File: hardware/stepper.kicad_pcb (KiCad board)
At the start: 4 copper layers, 40 x 40 mm, 125 parts, among them J101 USB-MINI-B-SMD, J102 DRILL, J103 DRILL, J104 DRILL, J105 DRILL, J401 STACK-UP-HIGH, J402 STACK-DOWN, J403 STACK-UP-HIGH, J404 STACK-DOWN, P201 black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

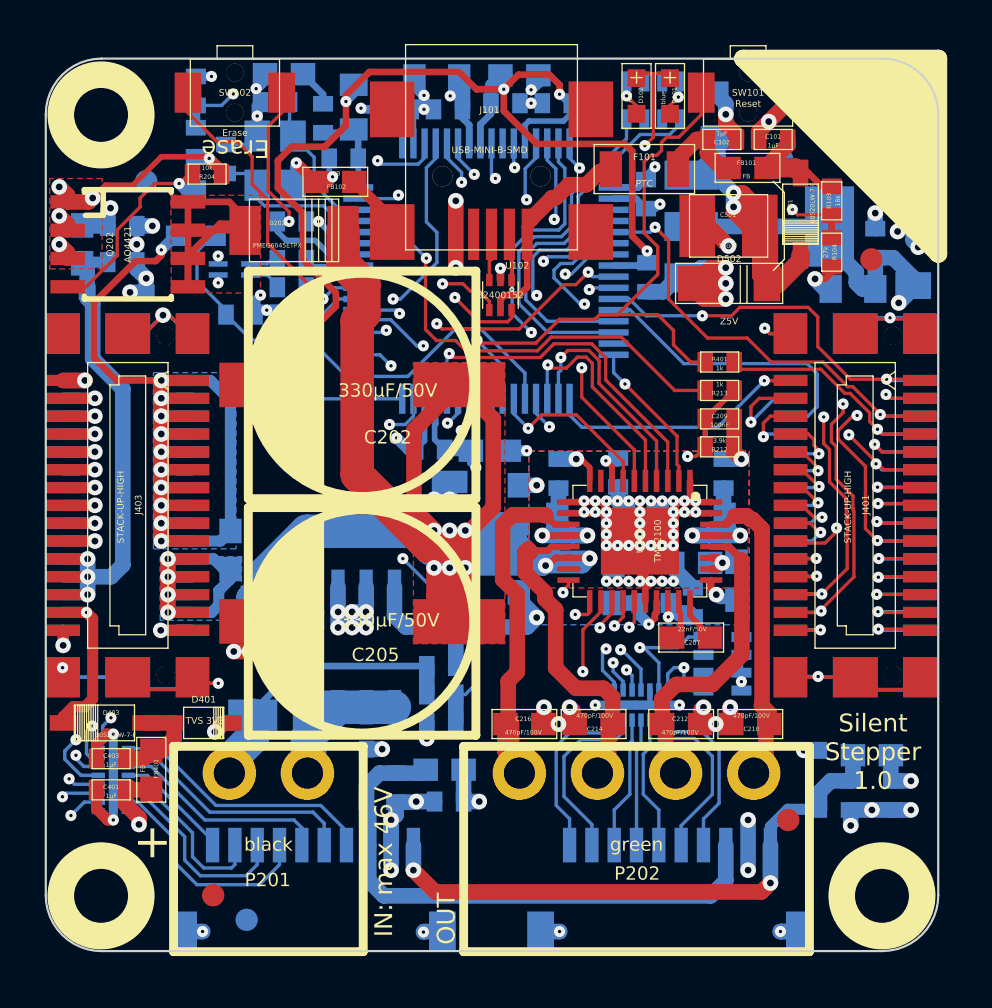
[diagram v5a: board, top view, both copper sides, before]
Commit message: remove motor capacitors
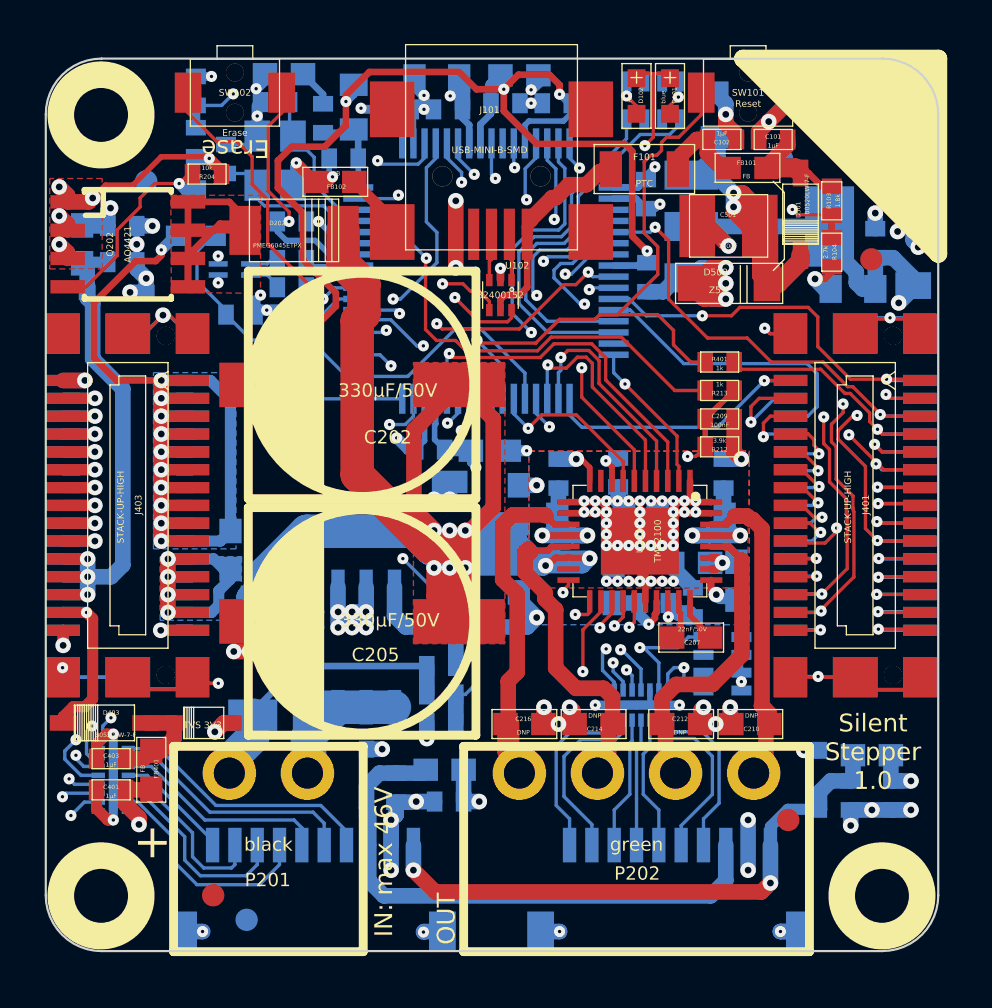
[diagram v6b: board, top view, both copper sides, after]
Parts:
- C210, C212, C214, C216: value 470pF/100V -> DNP
- R103: value 18k -> 1.8k
- R104: value 27k -> 2.7k
- turned D301 to 270 degrees
- turned D302 to 270 degrees
- turned D401 to 180 degrees
- turned D402 to 180 degrees
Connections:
- D301 pad 1: Net-(C303-Pad1) -> GND
- D301 pad 2: GND -> Net-(C303-Pad1)
- D302 pad 1: Net-(C304-Pad1) -> GND
- D302 pad 2: GND -> Net-(C304-Pad1)
- D401 pad 1: Net-(C403-Pad1) -> GND
- D401 pad 2: GND -> Net-(C403-Pad1)
- D402 pad 1: Net-(C404-Pad1) -> GND
- D402 pad 2: GND -> Net-(C404-Pad1)
- FILTER301 pad 8: Net-(FILTER301-Pad8) -> (no net)
- FILTER301 pad 9: Net-(FILTER301-Pad9) -> (no net)
- FILTER302 pad 8: Net-(FILTER302-Pad8) -> (no net)
- FILTER302 pad 9: Net-(FILTER302-Pad9) -> (no net)
- J101 pad 4: Net-(J101-Pad4) -> (no net)
- RP101 pad 2: Net-(RP101-Pad2) -> (no net)
- RP101 pad 3: Net-(RP101-Pad3) -> (no net)
- RP101 pad 6: Net-(RP101-Pad6) -> (no net)
- RP101 pad 7: Net-(RP101-Pad7) -> (no net)
- RP301 pad 6: Net-(RP301-Pad6) -> (no net)
- RP301 pad 7: Net-(RP301-Pad7) -> (no net)
- U101 pad 10: Net-(U101-Pad10) -> (no net)
- U101 pad 31: Net-(U101-Pad31) -> (no net)
- U101 pad 40: Net-(U101-Pad40) -> (no net)
- U101 pad 41: Net-(U101-Pad41) -> (no net)
- U101 pad 50: Net-(U101-Pad50) -> (no net)
- U202 pad 17: Net-(U202-Pad17) -> (no net)
- U202 pad 9: Net-(U202-Pad9) -> (no net)

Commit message: uncomitted hardware changes
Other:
- board text added: "check height"
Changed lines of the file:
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@@
     (area 125.845139 71.945139 283.420502 165.440043)
     (thickness 1.6002)
-    (drawings 63)
+    (drawings 64)
     (tracks 2561)
     (zones 0)
@@
   )
   (layers
-    (0 Vorderseite signal)
+    (0 Vorderseite signal hide)
     (1 GND signal hide)
     (2 VCC signal hide)
@@
     )
   )
+  (gr_text "check height" (at 155.75 99.75) (layer F.SilkS)
+    (effects (font (size 0.29972 0.29972) (thickness 0.07493)))
+  )
   (gr_text "Silent\nStepper\n1.0" (at 163.8 103.85) (layer F.SilkS)

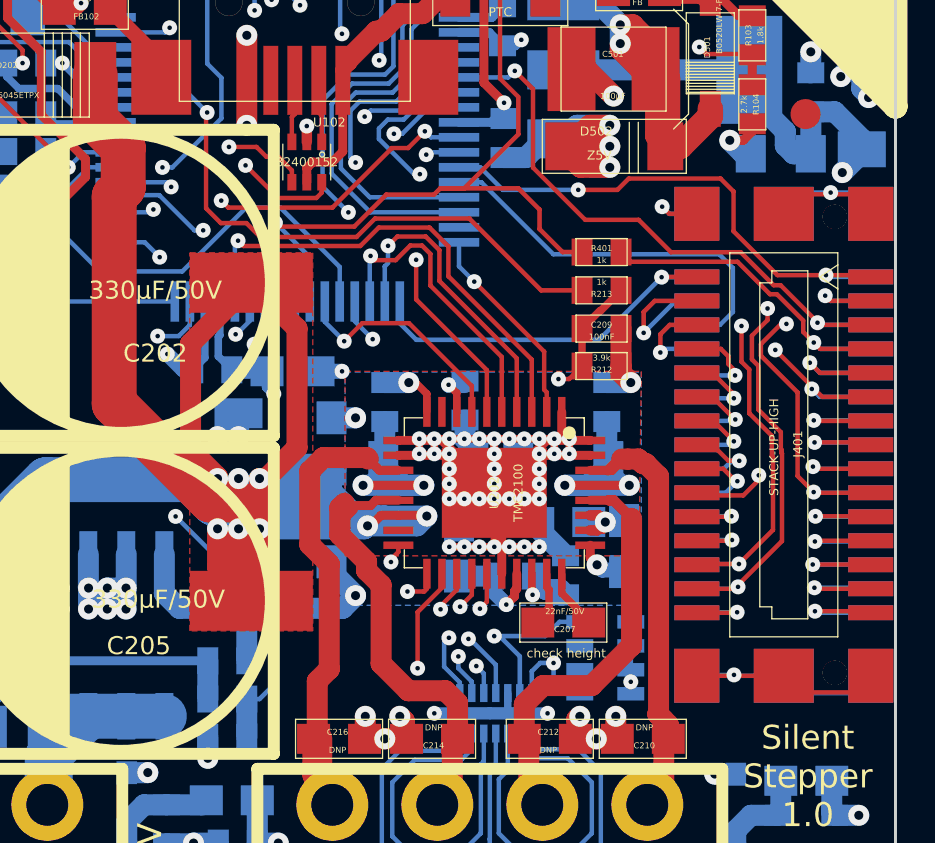
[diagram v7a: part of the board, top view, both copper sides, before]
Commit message: remove cfg3, add clk connection, imprv gnd routing, 3v3 switchable
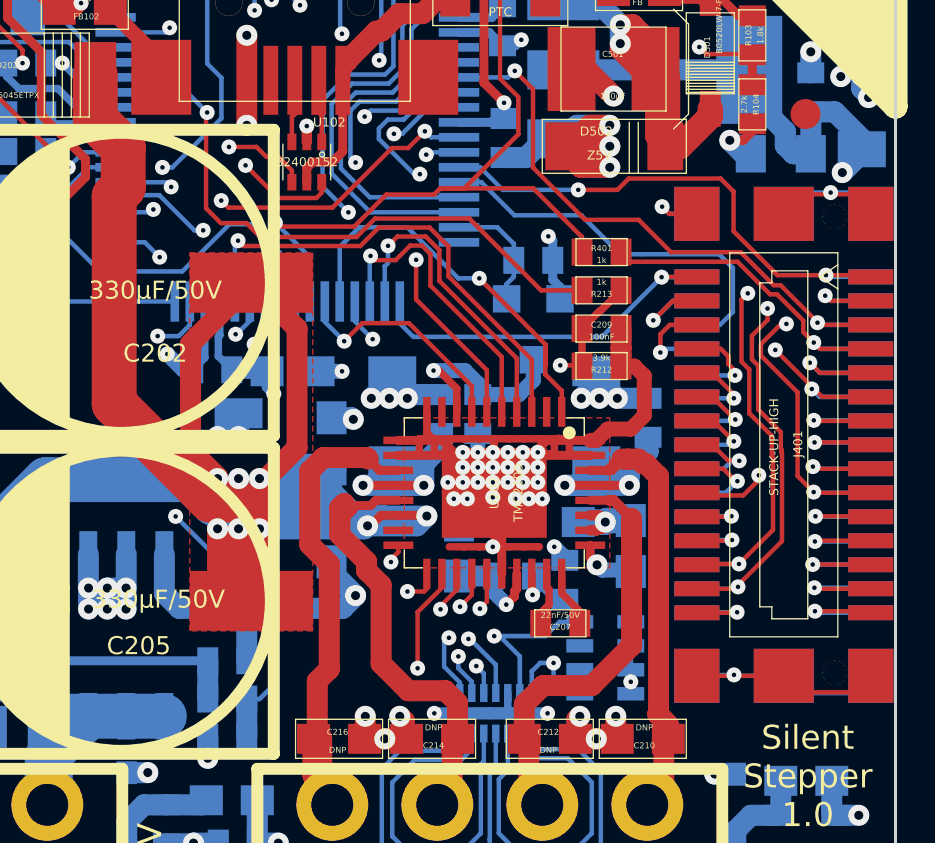
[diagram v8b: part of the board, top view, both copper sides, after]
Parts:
- added Q1: MOSFET_P, SOT23GDS, B.Cu at (154.7, 89.0)
- added R1: 10k, kicad-libraries:0402E, B.Cu at (154.7, 86.7)
- C207: footprint kicad-libraries:0603E -> kicad-libraries:0402E
- moved G*** 16.3 mm to (173.6, 82.8)
- moved R214 2.02 mm to (149.9, 91.8), turned to 270 degrees
- moved R215 1.96 mm to (156.8, 91.8), turned to 270 degrees
- moved C217 1.87 mm to (151.5, 91.8)
- moved C218 1.47 mm to (158.5, 91.9)
- moved C201 0.62 mm to (152.8, 91.8)
- moved C211 0.35 mm to (155.3, 95.4)
- moved C208 0.22 mm to (157.9, 96.2)
- moved C203 0.15 mm to (155.7, 97.3)
- moved C207 0.10 mm to (155.6, 98.8)
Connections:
- C201 pad 2: 3V3 -> Net-(C201-Pad2)
- U101 pad 31: (no net) -> PWR-SW-3V3
- U101 pad 32: PWR-CFG3 -> (no net)
- U101 pad 37: PWR-VSTACK-SW -> PWR-CLK
- U101 pad 41: (no net) -> PWR-VSTACK-SW
- U202 pad 1: STACK-PGND -> PWR-CLK
- U202 pad 2: PWR-CFG3 -> (no net)
- U202 pad 8: 3V3 -> Net-(C201-Pad2)
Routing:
- net STACK-PGND: track 219.2 -> 274.7 mm, vias 77 -> 70
- net PWR-CLK: track 0.00 -> 13.7 mm, vias 0 -> 1
- net PWR-CFG3: track 6.87 -> 0.00 mm, vias 1 -> 0
- net Net-(C201-Pad2): track 0.00 -> 6.56 mm, vias 0 -> 1
- net PWR-SW-3V3: track 0.00 -> 3.99 mm
- net 3V3: track 178.2 -> 181.7 mm
- net PWR-VSTACK-SW: track 21.9 -> 19.7 mm
- net Net-(C209-Pad2): track 18.7 -> 20.7 mm
- net VEE: track 95.8 -> 97.6 mm
- net Net-(C217-Pad2): track 8.11 -> 9.77 mm
- net Net-(C203-Pad1): track 2.46 -> 3.88 mm
- net STACK-SER-RXD: track 35.5 -> 36.8 mm
- net STACK-I2C-SCL/JTAG-TDO: track 24.4 -> 23.1 mm
- net STACK-SER-TXD: track 35.2 -> 35.8 mm
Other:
- board text removed: "check height"
